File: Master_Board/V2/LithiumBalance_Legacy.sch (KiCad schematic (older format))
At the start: 28 parts, among them Q101 BSS806NH6327XTSA1, Q102 2N7002P,215, Q103 BSS806NH6327XTSA1, Q104 BSS806NH6327XTSA1, U101 LMV321RILT, U102 LMV321RILT

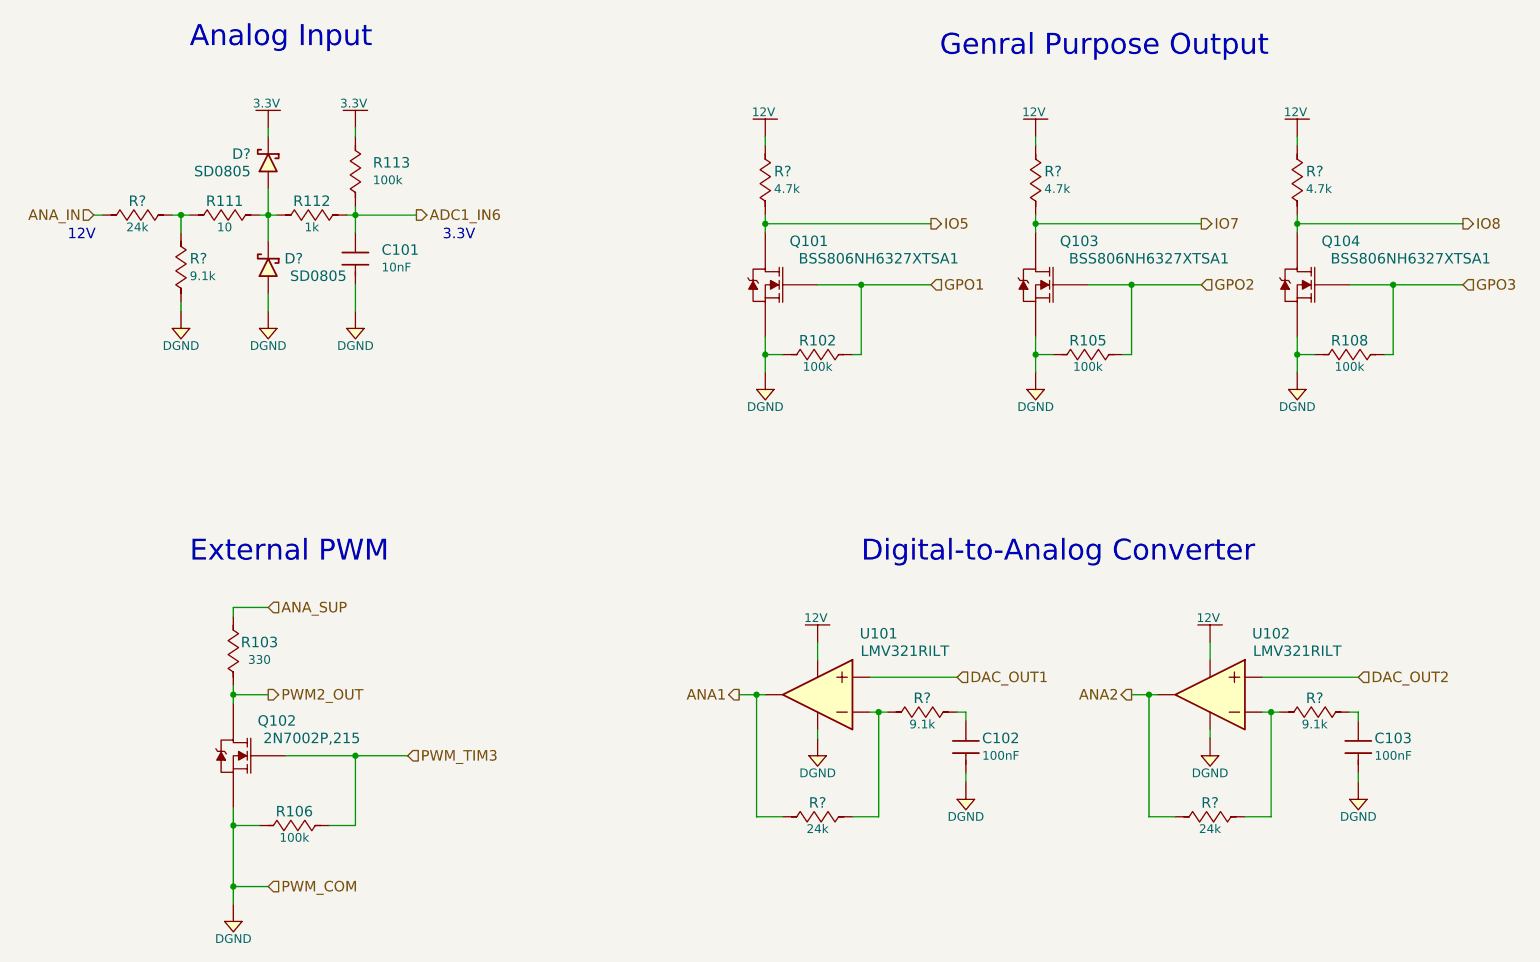
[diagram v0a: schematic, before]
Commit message: Place part in PCB
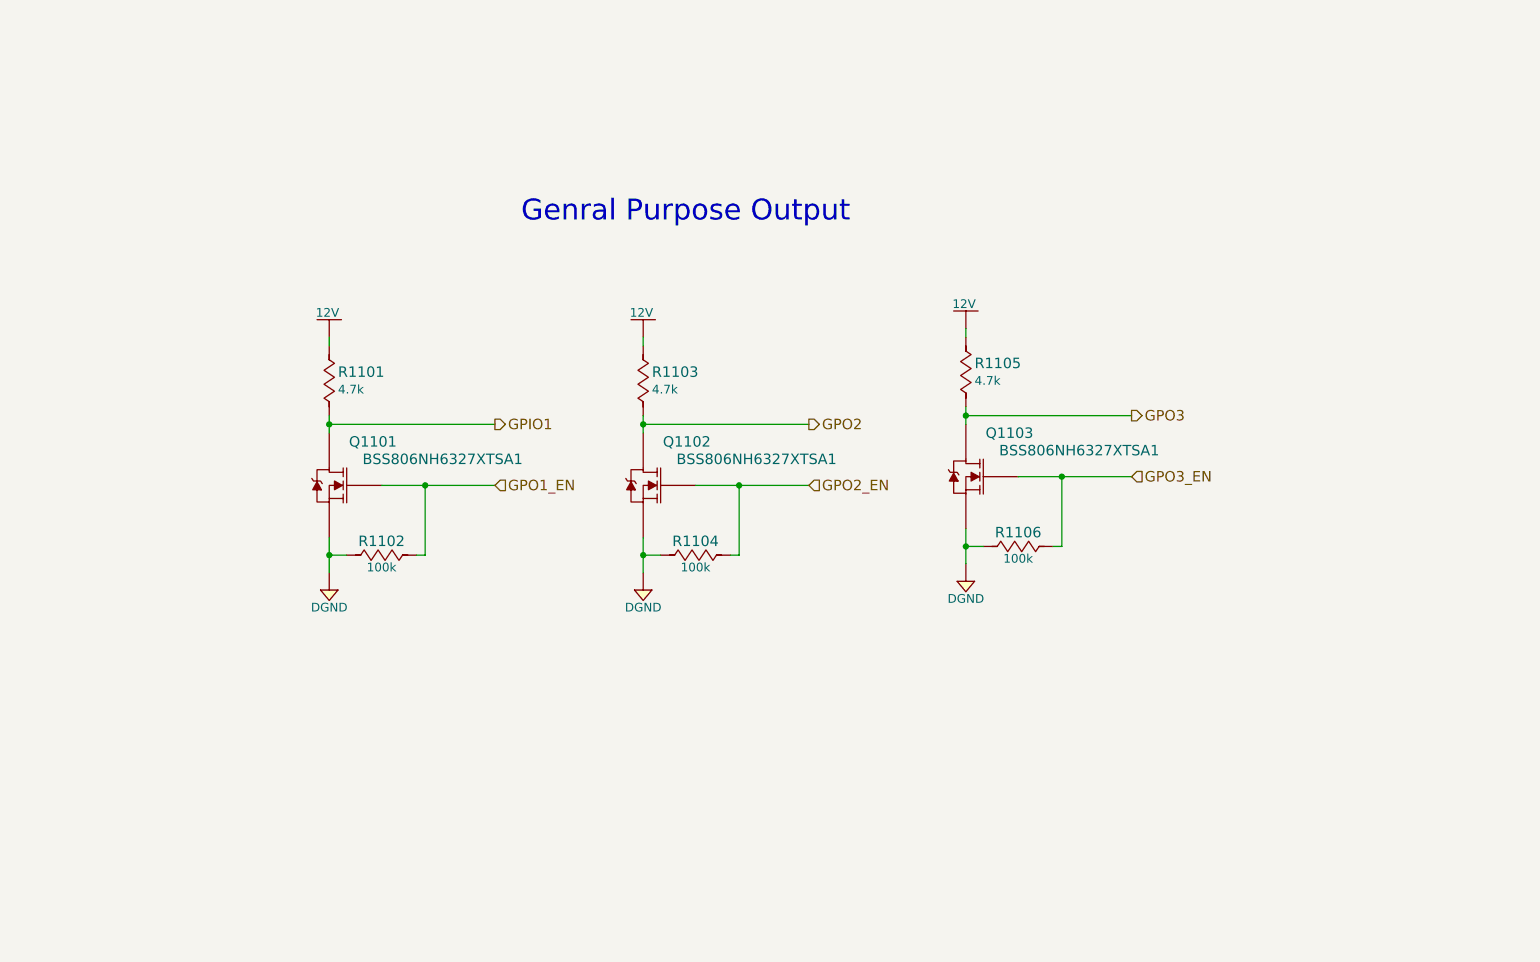
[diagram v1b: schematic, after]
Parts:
- removed C101: 885012207092, Capacitors:C0805, symbol 885012207092
- removed C102, C103: 885012207098, Capacitors:C0805, symbol 885012207098
- removed D? (x2): SD0805, Diodes:Diode_0805, symbol SD0805
- removed Q102: 2N7002P,215, IC:SOT-23-3, symbol 2N7002P,215
- removed R103: RC0805JR-07330RL, Resistors:R0805, symbol RC0805JR-07330RL
- removed R106, R113: RC0805JR-07100KL, Resistors:R0805, symbol RC0805JR-07100KL
- removed R111: RC0805JR-0710RL, Resistors:R0805, symbol RC0805JR-0710RL
- removed R112: RC0805JR-071KL, Resistors:R0805, symbol RC0805JR-071KL
- removed R? (x3): RC0805FR-0724KL, Resistors:R0805, symbol RC0805FR-0724KL
- removed R? (x3): RC0805FR-079K1L, Resistors:R0805, symbol RC0805FR-079K1L
- removed U101, U102: LMV321RILT, IC:SOT-23-5, symbol LMV321RILT
- gave numbers to parts that had none: 3
- renumbered Q101 to Q1101, Q103 to Q1102, Q104 to Q1103, R102 to R1102, R105 to R1104, R108 to R1106
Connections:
- net IO7 is gone; now on net GPO2: Q1102.3 (D), R1103.2
- net IO8 is gone; now on net GPO3: Q1103.3 (D), R1105.2
- net GPO2: no longer Q1102.1 (G), R1104.2
- net GPO3: no longer Q1103.1 (G), R1106.2
- net GPO1 renamed GPO1_EN
- net IO5 renamed GPIO1
- new net GPO2_EN: Q1102.1 (G), R1104.2
- new net GPO3_EN: Q1103.1 (G), R1106.2
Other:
- note removed: "12V"
- note removed: "3.3V"
- note removed: "Analog Input"
- note removed: "Digital-to-Analog Converter"
- note removed: "External PWM"
- moved on the sheet: Q1101, Q1102, Q1103, R1101, R1102, R1103, R1104, R1105, R1106
